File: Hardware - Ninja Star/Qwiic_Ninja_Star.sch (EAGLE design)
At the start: 9 parts, among them J1 QWIIC_RIGHT_ANGLE, J2 QWIIC_RIGHT_ANGLE, J3 QWIIC_RIGHT_ANGLE, J4 QWIIC_RIGHT_ANGLE

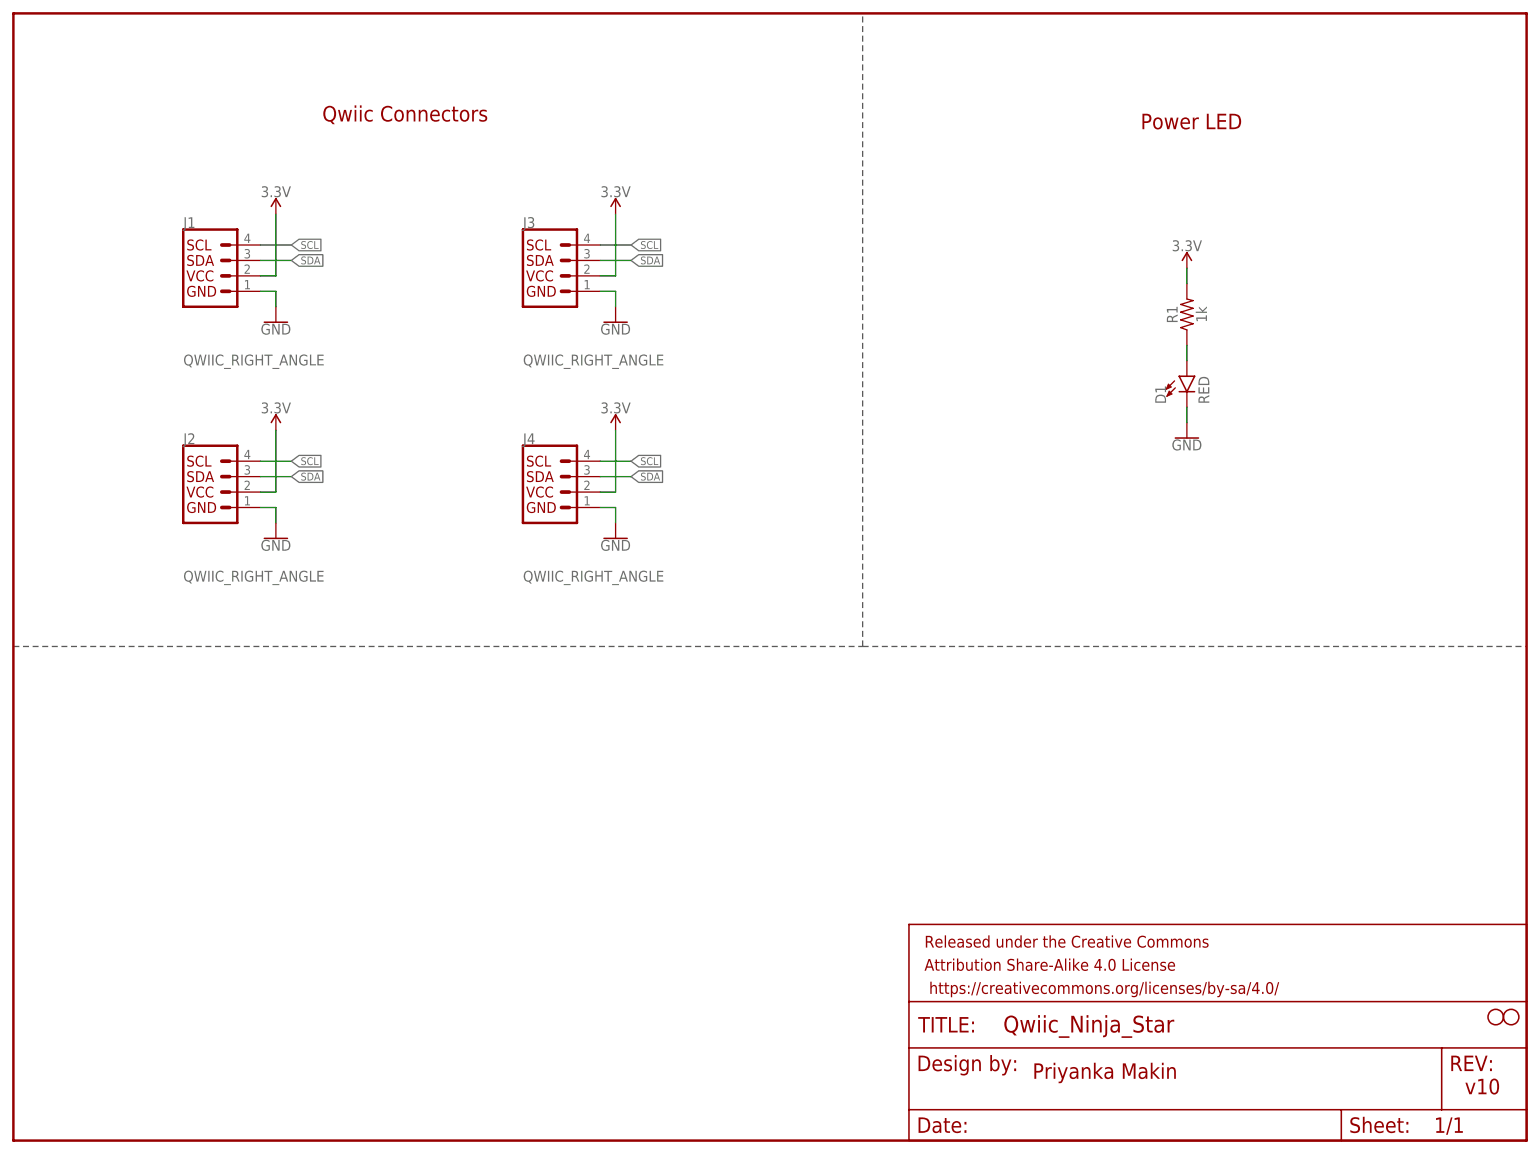
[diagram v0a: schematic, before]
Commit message: Ninja Star: Design Review Changes
Added jumper to PWR LED
Added fiducials
Added OSHW, qwiic, SF, and flame logo devices to schematic
Tried my best to move traces out from underneath screws
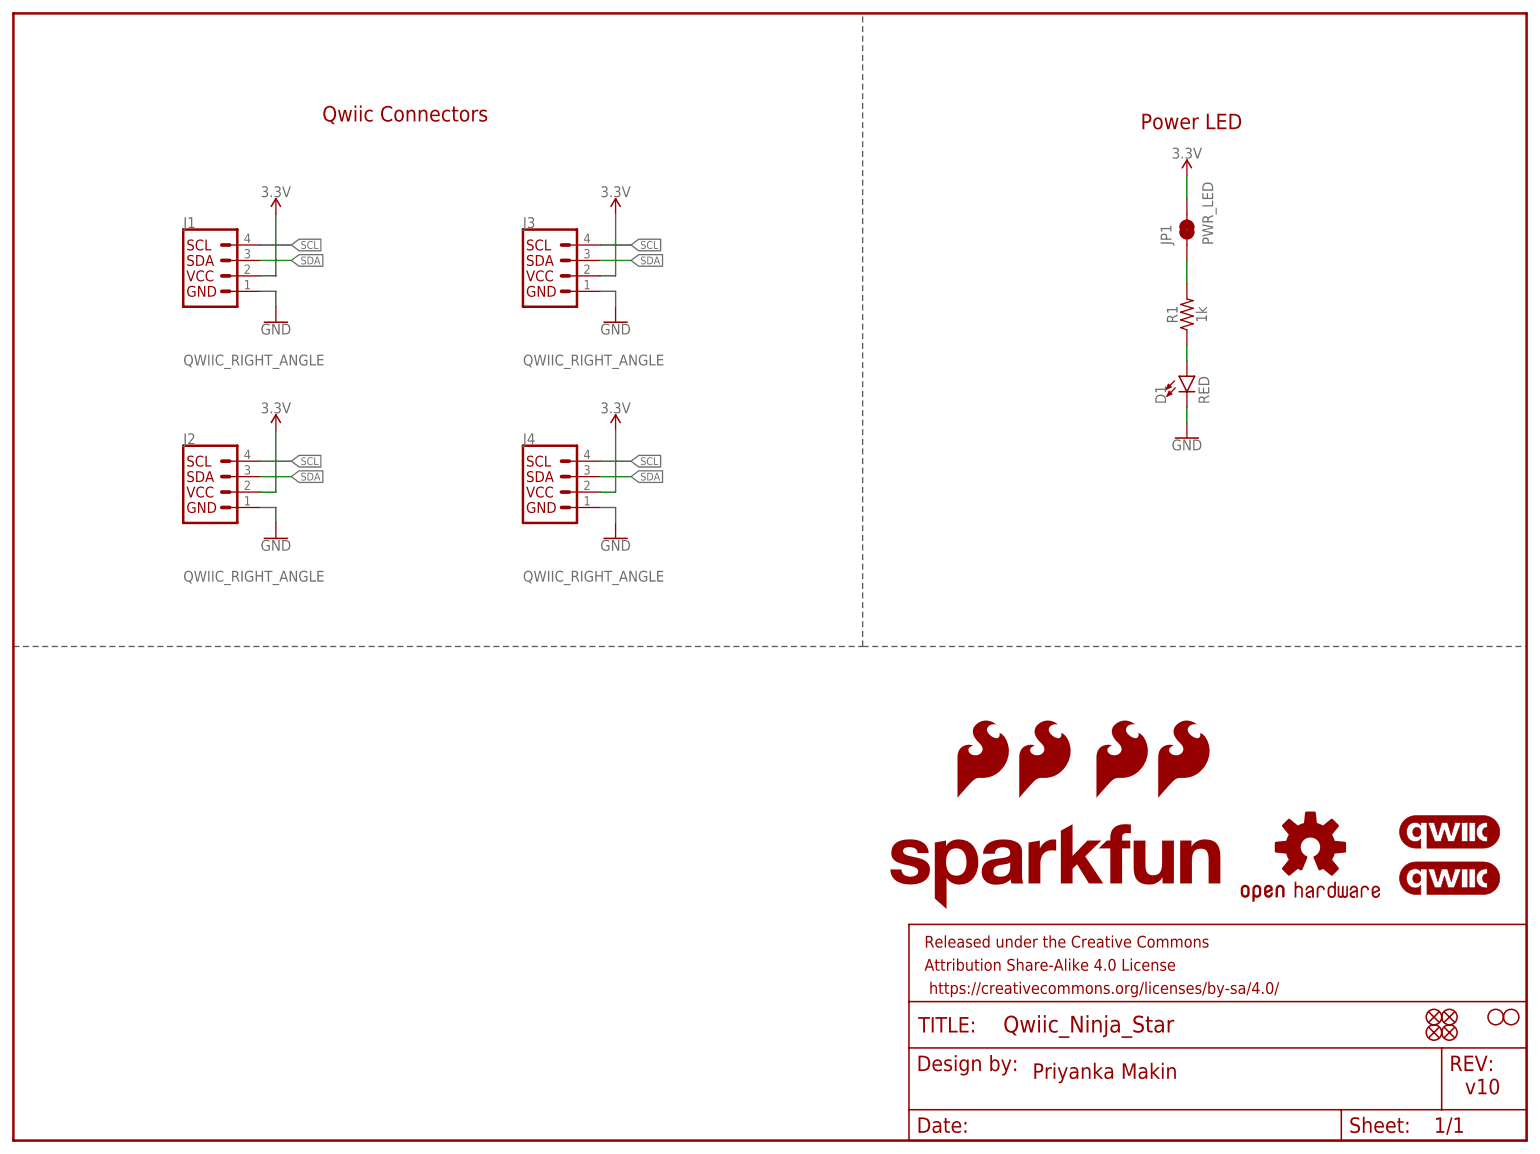
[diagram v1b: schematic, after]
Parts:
- added FD1, FD2, FD3, FD4: FIDUCIAL1X2, SparkFun-Aesthetics:FIDUCIAL1X2
- added JP1: PWR_LED, SparkFun-Jumpers:JUMPER-SMT_2_NC_TRACE_SILK
- added LOGO1, LOGO2: QWIIC_LOGO_5MM, SparkFun-Aesthetics:QWIIC_LOGO_5MM
- added LOGO3: OSHW-LOGOS, SparkFun-Aesthetics:OSHW-LOGOS
- added LOGO4: SFE_LOGO_NAME.2_INCH, SparkFun-Aesthetics:SFE_LOGO_NAME.2_INCH
- added LOGO5, LOGO6, LOGO7, LOGO8: SFE_LOGO_FLAME.1_INCH, SparkFun-Aesthetics:SFE_LOGO_FLAME.1_INCH
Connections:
- new net N$2: JP1.1, R1.2
- net 3.3V: now also JP1.2; no longer R1.2
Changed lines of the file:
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@@
 <setting verticaltext="up"/>
 </settings>
-<grid distance="0.05" unitdist="inch" unit="inch" style="lines" multiple="1" display="no" altdistance="0.005" altunitdist="inch" altunit="inch"/>
+<grid distance="0.1" unitdist="inch" unit="inch" style="lines" multiple="1" display="no" altdistance="0.01" altunitdist="inch" altunit="inch"/>
 <layers>
 <layer number="1" name="Top" color="4" fill="1" visible="no" active="no"/>
@@
 <part name="GND5" library="SparkFun-PowerSymbols" deviceset="GND" device=""/>
 <part name="SUPPLY5" library="SparkFun-PowerSymbols" deviceset="3.3V" device=""/>
+<part name="JP1" library="SparkFun-Jumpers" deviceset="JUMPER-SMT_2_NC_TRACE" device="_SILK" package3d_urn="urn:adsk.eagle:package:39281/1" value="PWR_LED"/>
+<part name="FD1" library="SparkFun-Aesthetics" deviceset="FIDUCIAL" device="1X2"/>
+<part name="FD2" library="SparkFun-Aesthetics" deviceset="FIDUCIAL" device="1X2"/>
+<part name="FD3" library="SparkFun-Aesthetics" deviceset="FIDUCIAL" device="1X2"/>
+<part name="FD4" library="SparkFun-Aesthetics" deviceset="FIDUCIAL" device="1X2"/>
+<part name="LOGO1" library="SparkFun-Aesthetics" deviceset="QWIIC_LOGO" device="_5MM"/>
+<part name="LOGO2" library="SparkFun-Aesthetics" deviceset="QWIIC_LOGO" device="_5MM"/>
+<part name="LOGO3" library="SparkFun-Aesthetics" deviceset="OSHW-LOGO" device="S"/>
+<part name="LOGO4" library="SparkFun-Aesthetics" deviceset="SFE_LOGO_NAME" device=".2_INCH"/>
+<part name="LOGO5" library="SparkFun-Aesthetics" deviceset="SFE_LOGO_FLAME" device=".1_INCH"/>
+<part name="LOGO6" library="SparkFun-Aesthetics" deviceset="SFE_LOGO_FLAME" device=".1_INCH"/>
+<part name="LOGO7" library="SparkFun-Aesthetics" deviceset="SFE_LOGO_FLAME" device=".1_INCH"/>
+<part name="LOGO8" library="SparkFun-Aesthetics" deviceset="SFE_LOGO_FLAME" device=".1_INCH"/>
 </parts>
 <sheets>
@@
 <attribute name="VALUE" x="193.04" y="115.316" size="1.778" layer="96" align="top-center"/>
 </instance>
-<instance part="SUPPLY5" gate="G$1" x="193.04" y="143.51" smashed="yes">
-<attribute name="VALUE" x="193.04" y="146.304" size="1.778" layer="96" align="bottom-center"/>
-</instance>
+<instance part="SUPPLY5" gate="G$1" x="193.04" y="158.75" smashed="yes">
+<attribute name="VALUE" x="193.04" y="161.544" size="1.778" layer="96" align="bottom-center"/>
+</instance>
+<instance part="JP1" gate="G$1" x="193.04" y="149.86" smashed="yes" rot="R90">
+<attribute name="NAME" x="190.5" y="147.32" size="1.778" layer="95" font="vector" rot="R90"/>
+<attribute name="VALUE" x="195.58" y="147.32" size="1.778" layer="96" font="vector" rot="R90" align="top-left"/>
+</instance>
+<instance part="FD1" gate="G$1" x="233.68" y="20.32" smashed="yes"/>
+<instance part="FD2" gate="G$1" x="236.22" y="20.32" smashed="yes"/>
+<instance part="FD3" gate="G$1" x="236.22" y="17.78" smashed="yes"/>
+<instance part="FD4" gate="G$1" x="233.68" y="17.78" smashed="yes"/>
+<instance part="LOGO1" gate="G$1" x="236.22" y="43.18" smashed="yes"/>
+<instance part="LOGO2" gate="G$1" x="236.22" y="50.8" smashed="yes"/>
+<instance part="LOGO3" gate="G$1" x="213.36" y="48.26" smashed="yes"/>
+<instance part="LOGO4" gate="G$1" x="142.24" y="38.1" smashed="yes"/>
+<instance part="LOGO5" gate="G$1" x="154.94" y="55.88" smashed="yes"/>
+<instance part="LOGO6" gate="G$1" x="165.1" y="55.88" smashed="yes"/>
+<instance part="LOGO7" gate="G$1" x="177.8" y="55.88" smashed="yes"/>
+<instance part="LOGO8" gate="G$1" x="187.96" y="55.88" smashed="yes"/>
 </instances>
 <busses>
@@
 </segment>
 <segment>
-<pinref part="R1" gate="G$1" pin="2"/>
+<pinref part="JP1" gate="G$1" pin="2"/>
 <pinref part="SUPPLY5" gate="G$1" pin="3.3V"/>
-<wire x1="193.04" y1="143.51" x2="193.04" y2="140.97" width="0.1524" layer="91"/>
+<wire x1="193.04" y1="154.94" x2="193.04" y2="158.75" width="0.1524" layer="91"/>
 </segment>
 </net>
@@
 <pinref part="R1" gate="G$1" pin="1"/>
 <wire x1="193.04" y1="128.27" x2="193.04" y2="130.81" width="0.1524" layer="91"/>
+</segment>
+</net>
+<net name="N$2" class="0">
+<segment>
+<pinref part="JP1" gate="G$1" pin="1"/>
+<pinref part="R1" gate="G$1" pin="2"/>
+<wire x1="193.04" y1="144.78" x2="193.04" y2="140.97" width="0.1524" layer="91"/>
 </segment>
 </net>
@@
 </schematic>
 </drawing>
+<compatibility>
+<note version="8.3" severity="warning">
+Since Version 8.3, EAGLE supports URNs for individual library
+assets (packages, symbols, and devices). The URNs of those assets
+will not be understood (or retained) with this version.
+</note>
+<note version="8.3" severity="warning">
+Since Version 8.3, EAGLE supports the association of 3D packages
+with devices in libraries, schematics, and board files. Those 3D
+packages will not be understood (or retained) with this version.
+</note>
+</compatibility>
 </eagle>
